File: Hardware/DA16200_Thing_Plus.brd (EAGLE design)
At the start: 22.9 x 58.4 mm, 103 parts, among them J2 THING_PLUS, J3 Qwiic, J5 USB C, J6 microSD, J7 CORTEX_JTAG_DEBUG_PTH_NS, Q1 20V/4.2A/52mΩ/1.4W, U1 DA16200MOD, U2 CH340E_MSOP10, U3 MCP73831, U5 4MB Flash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

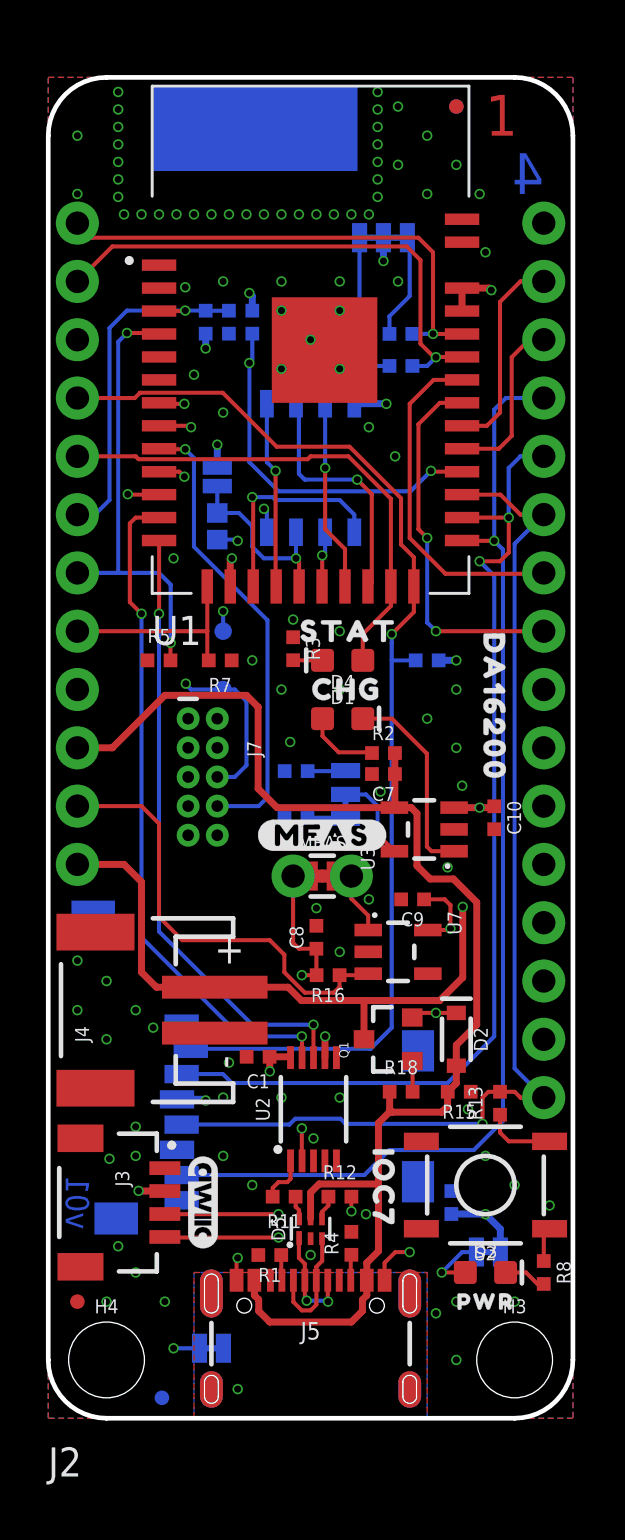
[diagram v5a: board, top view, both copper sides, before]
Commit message: Updates for Red's
* Added a NC jumper on the RTC_PWR_KEY pin to default to 3.3V. Users can cut the jumper to enter into sleep mode 1
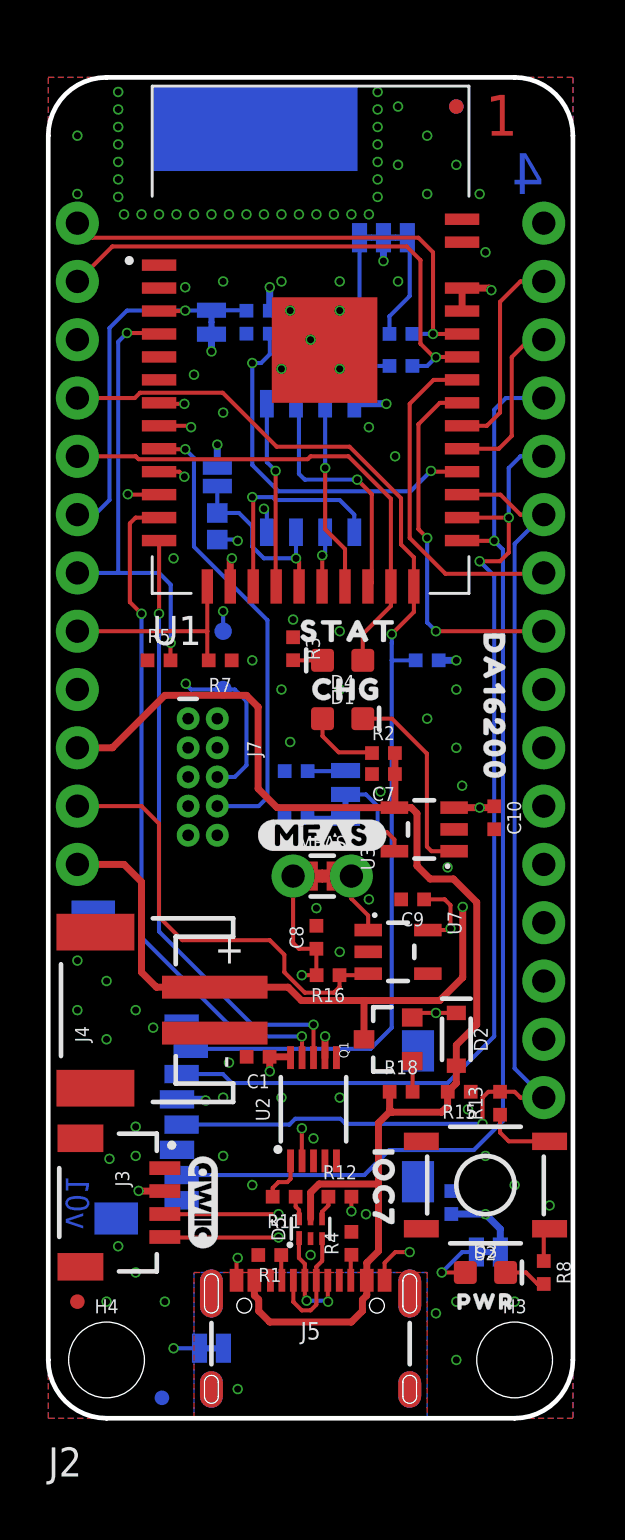
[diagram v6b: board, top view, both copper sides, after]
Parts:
- removed R9: DNP, SparkFun-Resistors:0402-TIGHT
- added RTC_PWR: JUMPER-SMT_2_NC_TRACE_SILK, SparkFun-Jumpers:SMT-JUMPER_2_NC_TRACE_SILK
- moved U$87 2.29 mm to (19.7, 26.2)
- moved U$88 2.03 mm to (19.6, 28.2)
- moved C3 0.76 mm to (8.64, 47.8)
- moved R20 0.76 mm to (9.65, 47.8)
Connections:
- net 3.3V: now also RTC_PWR.2; no longer R9.1
- net RTC_PWR_KEY: now also RTC_PWR.1; no longer R9.2
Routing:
- net RTC_PWR_KEY: track 15.8 -> 16.6 mm
- net SPI_CSB: track 23.7 -> 24.3 mm

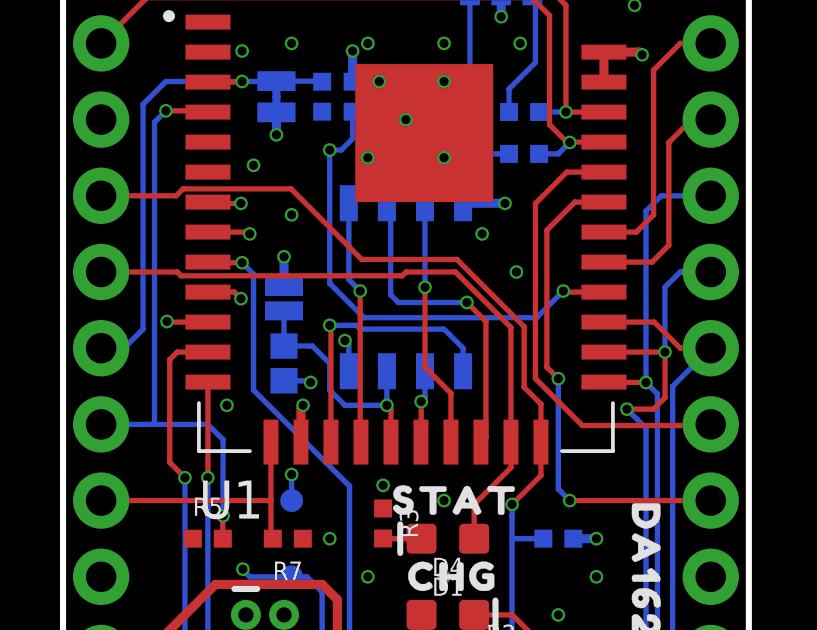
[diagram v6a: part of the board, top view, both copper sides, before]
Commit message: Remove external flash!
The "F" pins are the pins internally connecting the DA16200 with the in-module 4MB SFLASH!
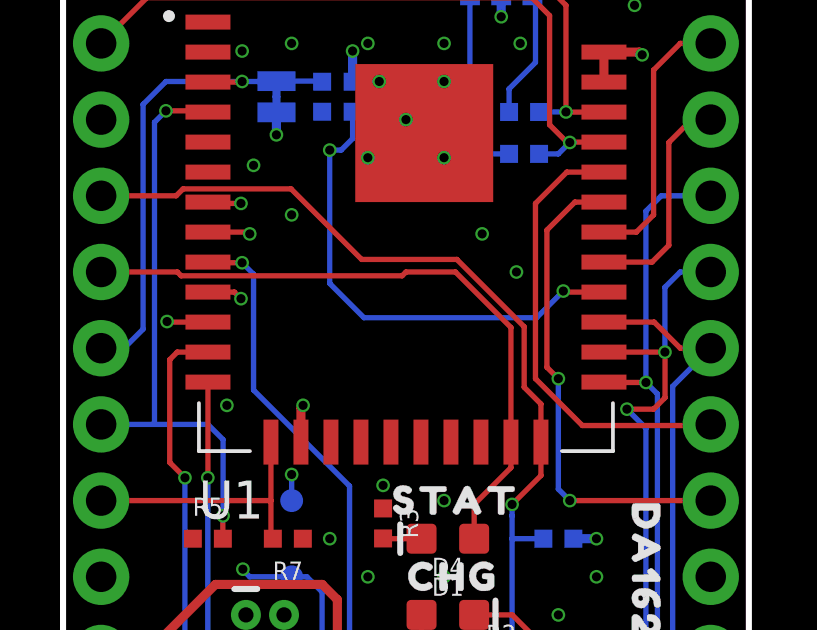
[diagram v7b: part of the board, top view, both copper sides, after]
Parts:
- removed R19: 10k, SparkFun-Resistors:0402
- removed U5: 4MB Flash, SparkFun-IC-Memory:SO08
- removed WP: JUMPER-SMT_2_NO_SILK, SparkFun-Jumpers:SMT-JUMPER_2_NO_SILK
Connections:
- removed net F_CLK: U1.21, U5.6
- removed net F_CSN: U1.16, U5.1
- removed net F_IO0: U1.19, U5.2
- removed net F_IO1: U1.17, U5.5
- removed net F_IO2: R19.2, U1.18, U5.3, WP.1
- removed net F_IO3: U1.20, U5.7
- net 3.3V: no longer U5.8, WP.2
- net GND: no longer R19.1, U5.4
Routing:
- net F_CLK: track 10.7 -> 0.00 mm, vias 1 -> 0
- net F_CSN: track 9.44 -> 0.00 mm, vias 1 -> 0
- net F_IO2: track 8.36 -> 0.00 mm, vias 1 -> 0
- net F_IO3: track 8.32 -> 0.00 mm, vias 1 -> 0
- net F_IO1: track 8.13 -> 0.00 mm, vias 1 -> 0
- net F_IO0: track 2.42 -> 0.00 mm, vias 1 -> 0
- net 3.3V: track 21.2 -> 18.8 mm, vias 14 -> 12
- net GND: track 7.67 -> 5.68 mm, vias 102 -> 100
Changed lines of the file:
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@@
 <layer number="38" name="bTest" color="7" fill="1" visible="no" active="yes"/>
 <layer number="39" name="tKeepout" color="4" fill="11" visible="no" active="yes"/>
-<layer number="40" name="bKeepout" color="1" fill="11" visible="yes" active="yes"/>
+<layer number="40" name="bKeepout" color="1" fill="11" visible="no" active="yes"/>
 <layer number="41" name="tRestrict" color="4" fill="10" visible="no" active="yes"/>
 <layer number="42" name="bRestrict" color="1" fill="10" visible="no" active="yes"/>
@@
 <attribute name="VALUE" x="7.112" y="4.191" size="0.6096" layer="28" font="vector" ratio="20" rot="MR180" align="top-center"/>
 </element>
-<element name="U5" library="SparkFun-IC-Memory" package="SO08" value="4MB Flash" x="11.43" y="41.402" smashed="yes" rot="MR0">
-<attribute name="NAME" x="14.605" y="41.402" size="0.6096" layer="26" font="vector" ratio="20" rot="MR90" align="bottom-center"/>
-<attribute name="PROD_ID" value="IC-12455" x="11.43" y="41.402" size="1.778" layer="28" font="vector" ratio="15" rot="MR0" display="off"/>
-<attribute name="VALUE" x="7.62" y="41.402" size="0.6096" layer="28" font="vector" ratio="20" rot="MR90" align="bottom-center"/>
-</element>
-<element name="R19" library="SparkFun-Resistors" package="0402" value="10k" x="7.366" y="38.862" smashed="yes" rot="MR90">
-<attribute name="NAME" x="7.928" y="38.862" size="0.6096" layer="26" font="vector" ratio="20" rot="MR90" align="bottom-center"/>
-<attribute name="PROD_ID" value="RES-14241" x="7.366" y="38.862" size="1.778" layer="28" font="vector" ratio="15" rot="MR90" display="off"/>
-<attribute name="VALUE" value="10k" x="6.804" y="38.862" size="0.6096" layer="28" font="vector" ratio="20" rot="MR90" align="top-center"/>
-</element>
-<element name="WP" library="SparkFun-Jumpers" package="SMT-JUMPER_2_NO_SILK" package3d_urn="urn:adsk.eagle:package:39279/1" value="JUMPER-SMT_2_NO_SILK" x="7.366" y="41.021" smashed="yes" rot="MR90">
-<attribute name="NAME" x="8.509" y="41.021" size="0.6096" layer="26" font="vector" ratio="20" rot="MR90" align="bottom-center"/>
-<attribute name="VALUE" x="6.223" y="41.021" size="0.6096" layer="28" font="vector" ratio="20" rot="MR90" align="top-center"/>
-</element>
 <element name="MEAS" library="SparkFun-Jumpers" package="COMBO-JUMPER_2_NC_TRACE" value="JUMPER-COMBO_2_NC_TRACE" x="11.938" y="23.622" smashed="yes">
 <attribute name="NAME" x="11.938" y="24.765" size="0.6096" layer="25" font="vector" ratio="20" align="bottom-center"/>
@@
 <contactref element="J7" pad="1"/>
 <contactref element="LED" pad="2"/>
-<contactref element="U5" pad="8"/>
-<contactref element="WP" pad="2"/>
 <wire x1="14.605" y1="51.435" x2="14.605" y2="50.419" width="0.3048" layer="16"/>
 <via x="14.605" y="50.419" extent="1-16" drill="0.3048"/>
@@
 <wire x1="19.213" y1="49.24" x2="19.304" y2="49.149" width="0.3048" layer="1"/>
 <via x="19.304" y="49.149" extent="1-16" drill="0.3048"/>
-<wire x1="13.335" y1="44.202" x2="14.726" y2="44.202" width="0.3048" layer="16"/>
-<wire x1="14.726" y1="44.202" x2="14.732" y2="44.196" width="0.3048" layer="16"/>
-<via x="14.732" y="44.196" extent="1-16" drill="0.3048"/>
-<wire x1="7.366" y1="41.4274" x2="7.366" y2="42.418" width="0.3048" layer="16"/>
-<via x="7.366" y="42.418" extent="1-16" drill="0.3048"/>
 <wire x1="7.93" y1="36.24" x2="7.93" y2="37.394" width="0.3048" layer="1"/>
 <wire x1="7.93" y1="37.394" x2="8.001" y2="37.465" width="0.3048" layer="1"/>
@@
 <contactref element="R4" pad="2"/>
 <contactref element="R1" pad="2"/>
-<contactref element="U5" pad="4"/>
-<contactref element="R19" pad="1"/>
 <via x="5.969" y="49.276" extent="1-16" drill="0.3048"/>
 <via x="10.541" y="48.26" extent="1-16" drill="0.3048"/>
@@
 <via x="12.7" y="45.72" extent="1-16" drill="0.3048"/>
 <via x="10.16" y="45.72" extent="1-16" drill="0.3048"/>
-<via x="9.398" y="39.624" extent="1-16" drill="0.3048"/>
-<wire x1="9.525" y1="38.602" x2="9.525" y2="39.497" width="0.1778" layer="16"/>
-<wire x1="9.525" y1="39.497" x2="9.398" y2="39.624" width="0.1778" layer="16"/>
 <via x="8.89" y="33.02" extent="1-16" drill="0.3048"/>
 <via x="10.668" y="34.798" extent="1-16" drill="0.3048"/>
@@
 <via x="10.16" y="13.97" extent="1-16" drill="0.3048"/>
 <via x="7.62" y="13.97" extent="1-16" drill="0.3048"/>
-<wire x1="7.366" y1="38.282" x2="8.2" y2="38.282" width="0.1778" layer="16"/>
-<wire x1="8.2" y1="38.282" x2="8.255" y2="38.227" width="0.1778" layer="16"/>
-<via x="8.255" y="38.227" extent="1-16" drill="0.3048"/>
 </signal>
 <signal name="V_USB">
@@
 <wire x1="13.081" y1="41.91" x2="14.93" y2="40.061" width="0.1778" layer="1"/>
 </signal>
-<signal name="F_CLK">
-<contactref element="U1" pad="21"/>
-<contactref element="U5" pad="6"/>
-<wire x1="10.795" y1="44.202" x2="10.922" y2="44.075" width="0.1778" layer="16"/>
-<wire x1="10.922" y1="44.075" x2="10.922" y2="41.148" width="0.1778" layer="16"/>
-<wire x1="11.176" y1="40.894" x2="10.922" y2="41.148" width="0.1778" layer="16"/>
-<wire x1="11.176" y1="40.894" x2="13.462" y2="40.894" width="0.1778" layer="16"/>
-<via x="13.462" y="40.894" extent="1-16" drill="0.3048"/>
-<wire x1="13.93" y1="36.24" x2="14.097" y2="36.407" width="0.1778" layer="1"/>
-<wire x1="13.462" y1="40.894" x2="14.097" y2="40.259" width="0.1778" layer="1"/>
-<wire x1="14.097" y1="40.259" x2="14.097" y2="36.407" width="0.1778" layer="1"/>
-</signal>
-<signal name="F_CSN">
-<contactref element="U1" pad="16"/>
-<contactref element="U5" pad="1"/>
-<wire x1="13.335" y1="38.602" x2="13.335" y2="39.37" width="0.1778" layer="16"/>
-<wire x1="13.335" y1="39.37" x2="12.7" y2="40.005" width="0.1778" layer="16"/>
-<wire x1="12.7" y1="40.005" x2="9.906" y2="40.005" width="0.1778" layer="16"/>
-<wire x1="9.906" y1="40.005" x2="9.779" y2="40.132" width="0.1778" layer="16"/>
-<wire x1="9.779" y1="40.132" x2="8.89" y2="40.132" width="0.1778" layer="16"/>
-<via x="8.89" y="40.132" extent="1-16" drill="0.3048"/>
-<wire x1="8.89" y1="40.132" x2="8.93" y2="40.092" width="0.1778" layer="1"/>
-<wire x1="8.93" y1="40.092" x2="8.93" y2="36.24" width="0.1778" layer="1"/>
-</signal>
-<signal name="F_IO0">
-<contactref element="U1" pad="19"/>
-<contactref element="U5" pad="2"/>
-<wire x1="12.065" y1="38.602" x2="12.065" y2="37.719" width="0.1778" layer="16"/>
-<wire x1="12.065" y1="37.719" x2="11.938" y2="37.592" width="0.1778" layer="16"/>
-<via x="11.938" y="37.592" extent="1-16" drill="0.3048"/>
-<wire x1="11.938" y1="37.592" x2="11.938" y2="36.248" width="0.1778" layer="1"/>
-<wire x1="11.938" y1="36.248" x2="11.93" y2="36.24" width="0.1778" layer="1"/>
-</signal>
-<signal name="F_IO1">
-<contactref element="U1" pad="17"/>
-<contactref element="U5" pad="5"/>
-<wire x1="9.525" y1="44.202" x2="9.525" y2="41.656" width="0.1778" layer="16"/>
-<wire x1="9.525" y1="41.656" x2="9.906" y2="41.275" width="0.1778" layer="16"/>
-<via x="9.906" y="41.275" extent="1-16" drill="0.3048"/>
-<wire x1="9.906" y1="41.275" x2="9.906" y2="36.264" width="0.1778" layer="1"/>
-<wire x1="9.906" y1="36.264" x2="9.93" y2="36.24" width="0.1778" layer="1"/>
-</signal>
-<signal name="F_IO2">
-<contactref element="U1" pad="18"/>
-<contactref element="U5" pad="3"/>
-<contactref element="WP" pad="1"/>
-<contactref element="R19" pad="2"/>
-<wire x1="10.795" y1="38.602" x2="10.795" y2="37.465" width="0.1778" layer="16"/>
-<via x="10.795" y="37.465" extent="1-16" drill="0.3048"/>
-<wire x1="10.795" y1="37.465" x2="10.93" y2="37.33" width="0.1778" layer="1"/>
-<wire x1="10.93" y1="37.33" x2="10.93" y2="36.24" width="0.1778" layer="1"/>
-<wire x1="7.366" y1="39.442" x2="7.366" y2="40.6146" width="0.1778" layer="16"/>
-<wire x1="10.795" y1="37.465" x2="9.398" y2="37.465" width="0.1778" layer="16"/>
-<wire x1="9.398" y1="37.465" x2="8.89" y2="37.973" width="0.1778" layer="16"/>
-<wire x1="8.89" y1="38.862" x2="8.89" y2="37.973" width="0.1778" layer="16"/>
-<wire x1="7.366" y1="39.442" x2="8.31" y2="39.442" width="0.1778" layer="16"/>
-<wire x1="8.31" y1="39.442" x2="8.89" y2="38.862" width="0.1778" layer="16"/>
-</signal>
-<signal name="F_IO3">
-<contactref element="U1" pad="20"/>
-<contactref element="U5" pad="7"/>
-<wire x1="12.065" y1="44.202" x2="12.065" y2="41.402" width="0.1778" layer="16"/>
-<via x="12.065" y="41.402" extent="1-16" drill="0.3048"/>
-<wire x1="12.93" y1="37.87" x2="12.065" y2="38.735" width="0.1778" layer="1"/>
-<wire x1="12.065" y1="41.402" x2="12.065" y2="38.735" width="0.1778" layer="1"/>
-<wire x1="12.93" y1="37.87" x2="12.93" y2="36.24" width="0.1778" layer="1"/>
-</signal>
 <signal name="N$22">

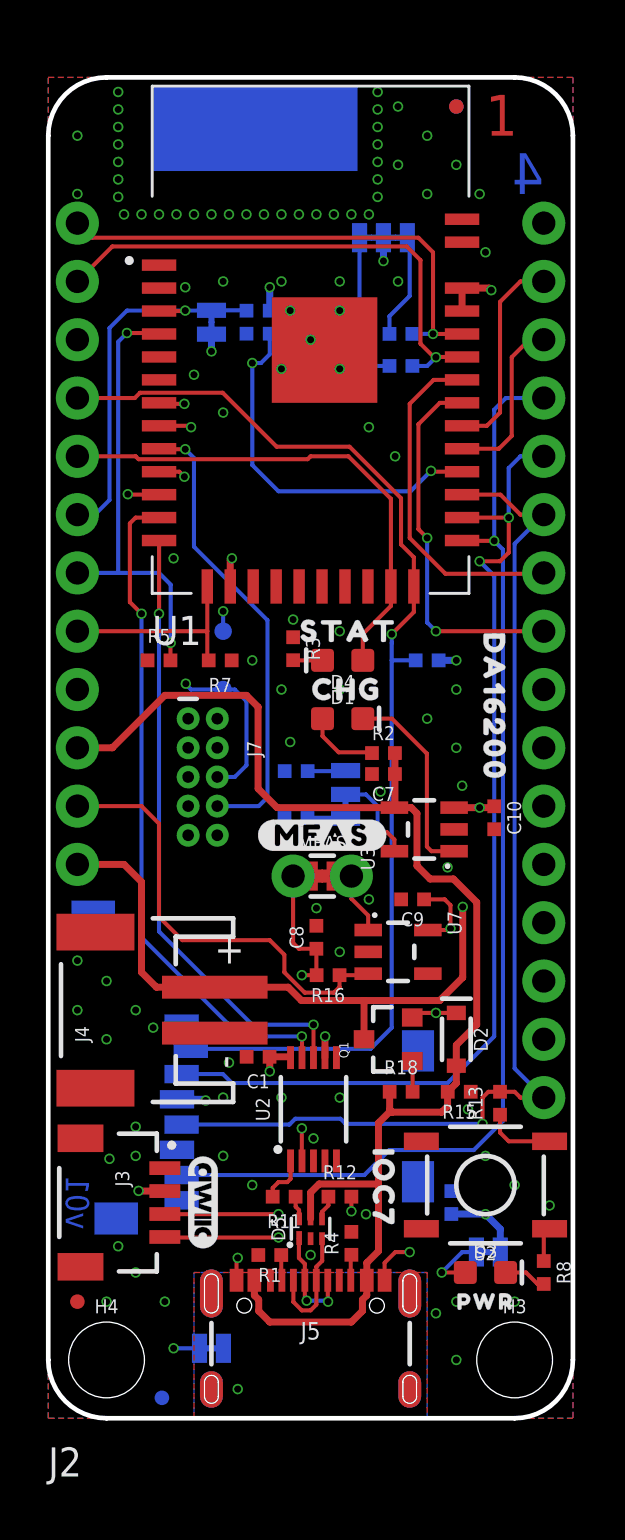
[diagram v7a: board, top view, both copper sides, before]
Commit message: Add SPDT switch for RTC_PWR_KEY
Added surface mount switch to pull RTC_PWR_KEY to 3.3V or GND
* Needed to extend the length of board by one grid space
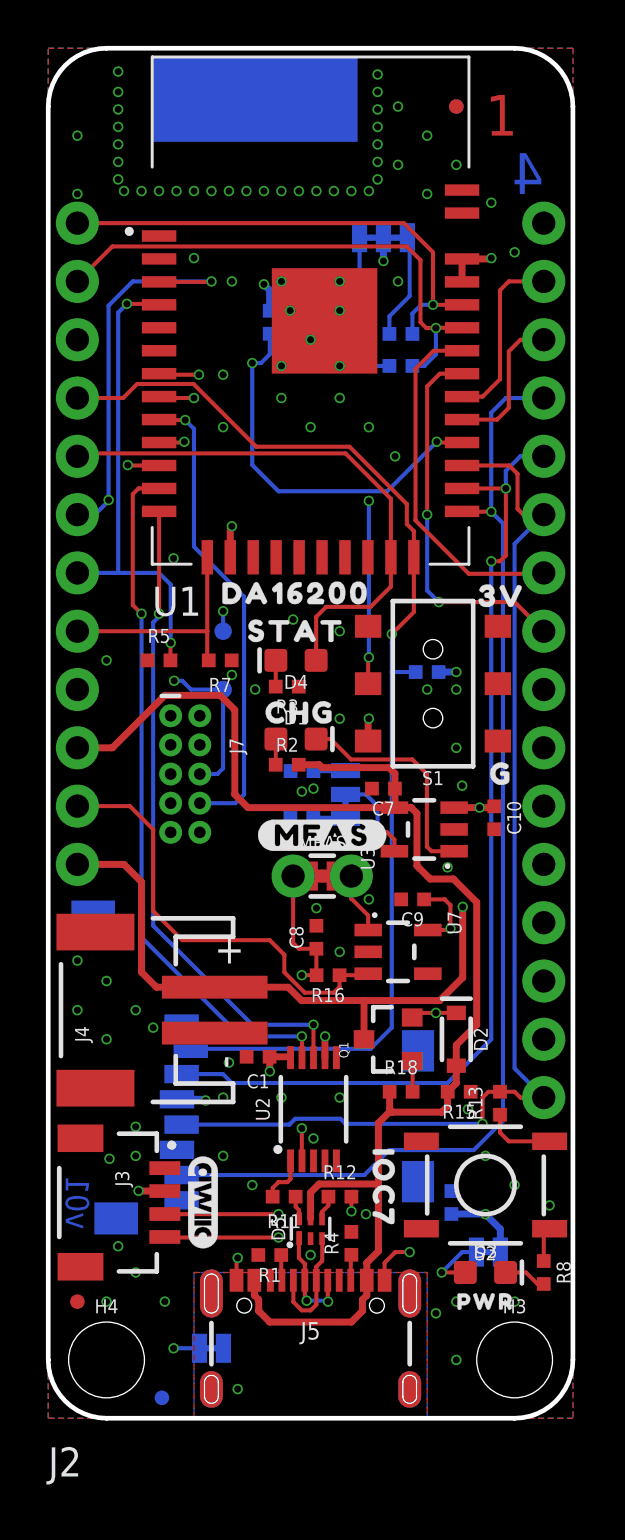
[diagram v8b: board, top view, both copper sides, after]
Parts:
- removed C3: DNP, SparkFun-Capacitors:0402-TIGHT
- removed RTC_PWR: JUMPER-SMT_2_NC_TRACE_SILK, SparkFun-Jumpers:SMT-JUMPER_2_NC_TRACE_SILK
- removed U$83: (no value), output:WP0
- added S1: (no value), SparkFun-Switches:SWITCH_DPDT_SMD_AYZ0202
- added U$4: (no value), output:G0
- added U$9: (no value), output:3V0
- moved U$81 12.6 mm to (6.86, 35.9), turned to 0 degrees
- moved R2 4.22 mm to (10.4, 28.5)
- moved U$1 2.29 mm to (8.00, 34.3)
- moved U$2 2.27 mm to (8.76, 30.7)
- moved D1 2.22 mm to (10.8, 29.6)
- moved D4 2.03 mm to (10.8, 33.0)
- moved R3 1.67 mm to (10.4, 31.9), turned to 180 degrees
- moved U1 1.27 mm to (11.4, 48.3)
- moved J7 0.77 mm to (5.97, 28.1)
- moved U$86 0.77 mm to (15.1, 29.7)
- moved C7 0.64 mm to (14.6, 27.4)
- moved R21 0.51 mm to (16.5, 32.5)
- moved R14 0.25 mm to (11.1, 28.2)
- moved R6 0.25 mm to (11.0, 26.2)
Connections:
- net 3.3V: now also S1.1; no longer RTC_PWR.2
- net GND: now also S1.3; no longer C3.2
- net RTC_PWR_KEY: now also S1.2; no longer C3.1, RTC_PWR.1
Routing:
- net RTC_PWR_KEY: track 16.6 -> 36.6 mm, vias 1 -> 4
- net V_USB: track 60.6 -> 64.1 mm
- net N$17: track 3.22 -> 1.12 mm
- net STAT_LED: track 22.1 -> 24.1 mm
- net U0RXI: track 26.9 -> 28.4 mm
- net !RESET!/SPI_CLK: track 47.7 -> 49.1 mm
- net TMS: track 17.1 -> 18.5 mm
- net I2C_SCL: track 71.8 -> 73.2 mm
- net TCLK: track 15.9 -> 17.2 mm
- net RTC_WAKE1: track 19.6 -> 20.9 mm
- net HDR_RTC_WAKE2: track 9.03 -> 10.3 mm
- net N$9: track 8.75 -> 9.89 mm
- net U1RXI: track 7.54 -> 6.44 mm
- net U0TXO: track 29.3 -> 30.4 mm
- net U1TXO: track 8.99 -> 7.91 mm
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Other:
- board size 22.9 x 58.4 mm -> 22.9 x 59.7 mm
